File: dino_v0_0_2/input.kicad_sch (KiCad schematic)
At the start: 13 parts, among them SW1 SW_DIP_x08, U76 74LS138

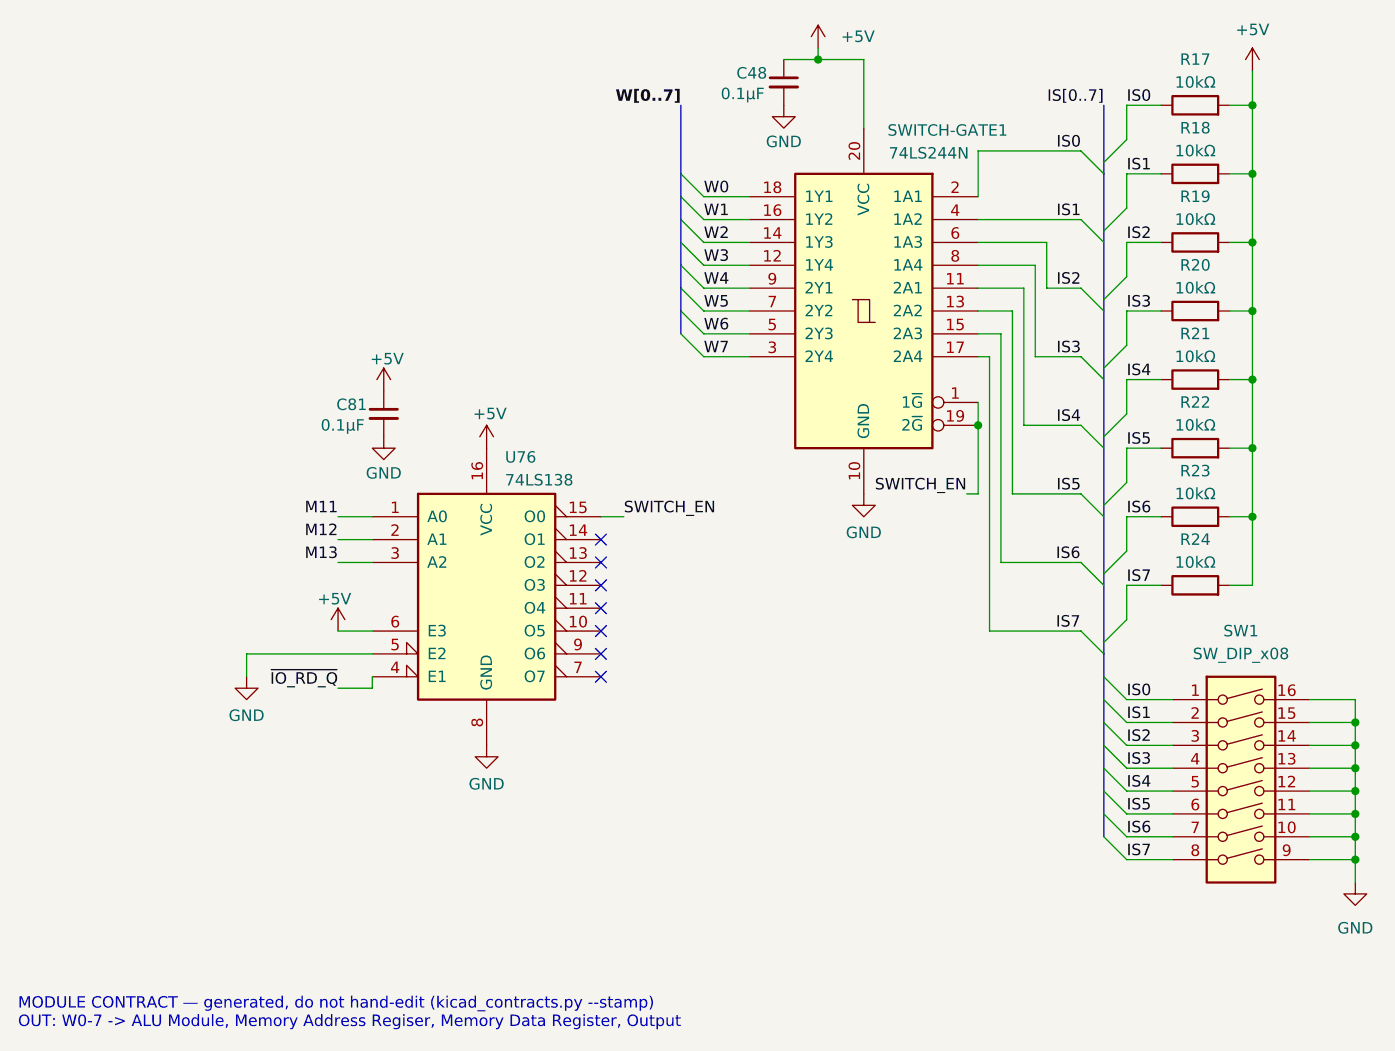
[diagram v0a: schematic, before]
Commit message: feat(kicad): footprints, power sheet, global labels, PCB draft
Every symbol gets a stock THT footprint (plain DIP, no sockets, so the
3D render shows ICs). New Power sheet: 24-pin ATX header for a picoPSU,
rails +5V/+3.3V/+12V/-12V/GND only; no -5V exists on any ATX unit since
2003, none drawn. PS_ON# on a 2-pin header.

Cross-sheet labels become global labels. KiCad joined nothing between
sheets before: 122 base names were split per sheet, ERC saw 90 undriven
inputs whose driver sat one sheet away, and the PCB ratsnest stopped at
every sheet boundary. Proof: KiCad's netlist after equals a name-join of
its netlist before plus the 15 CW alias pairs, pin for pin.

kicad_contracts took a node's sheet from the net name's /Sheet/ prefix;
global nets have none, so it emitted an empty contracts doc. Sheet now
comes from the component's own path; the doc regenerates with zero diff.

ERC 477 -> 2. Real fixes: ROM I/O pins input -> tri_state, '382 GND pin
power_out -> power_in, four orphan symbols rehomed to project lib `dino`,
one stub wire. 133 by-design warnings excluded by uuid ('245 readback on
counter Q, alias stubs, probe-point labels); the two left are bus
signals the peripheral bus sheet will consume.

PCB draft: 198 footprints placed per sheet, all pads netted, no tracks.

Co-Authored-By: Claude Fable 5.1 <noreply@anthropic.com>
Claude-Session: https://claude.ai/code/session_018irreFHb1xEykW5kCD26ow
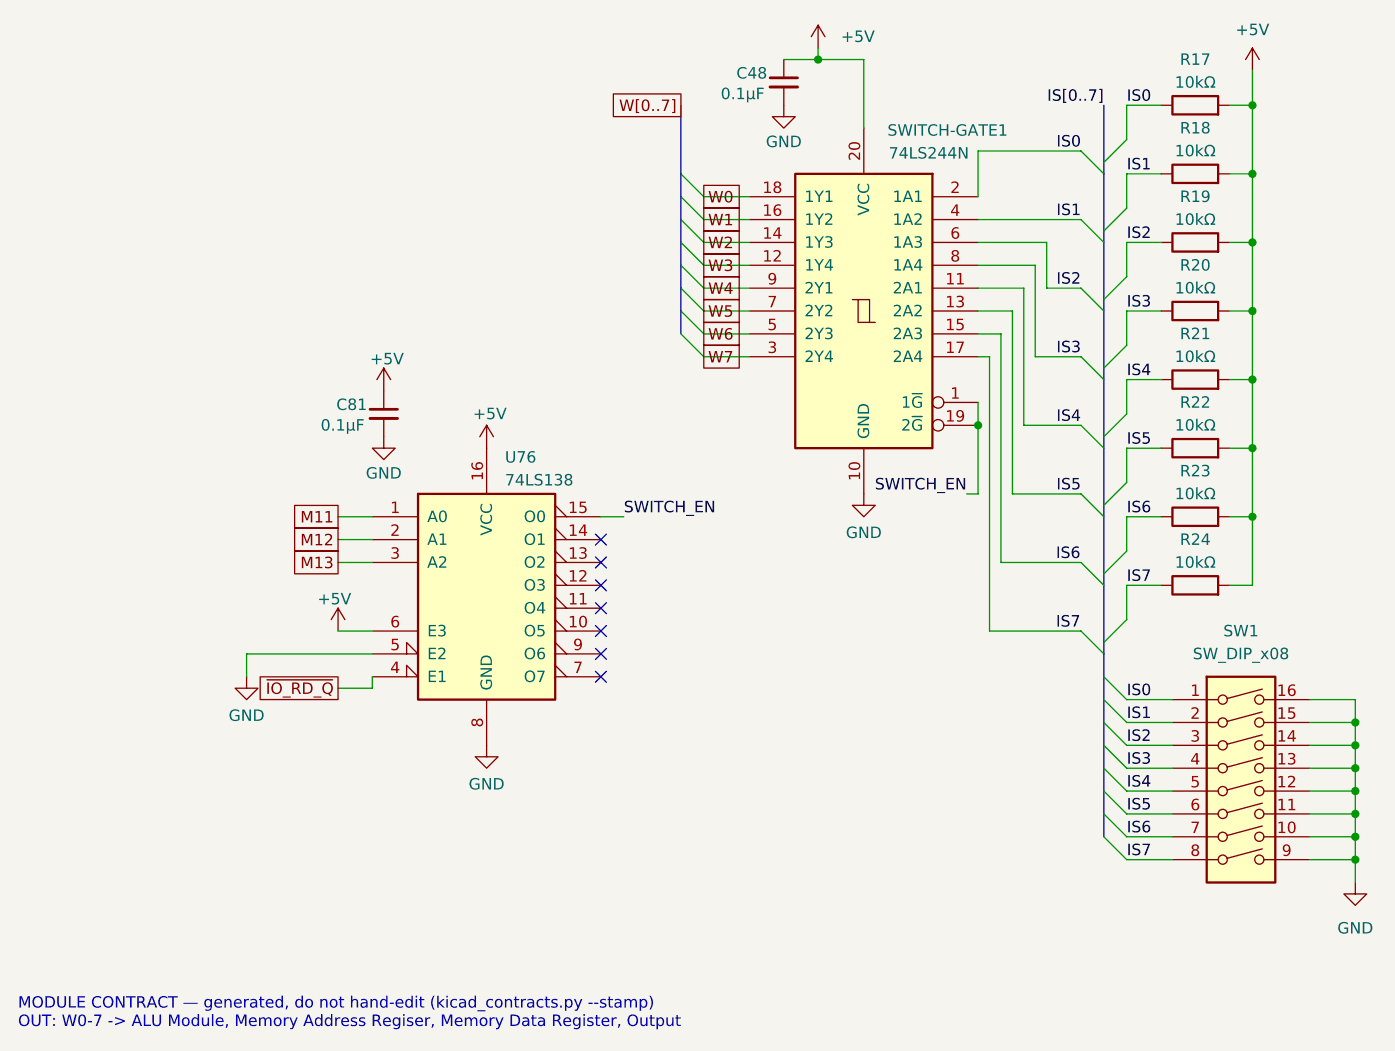
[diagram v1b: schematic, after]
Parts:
- C48, C81: footprint (none) -> Capacitor_THT:C_Disc_D5.0mm_W2.5mm_P2.50mm
- R17, R18, R19, R20, R21, R22, R23, R24: footprint (none) -> Resistor_THT:R_Axial_DIN0207_L6.3mm_D2.5mm_P10.16mm_Horizontal
- SW1: footprint (none) -> Button_Switch_THT:SW_DIP_SPSTx08_Slide_9.78x22.5mm_W7.62mm_P2.54mm
- SWITCH-GATE1: footprint (none) -> Package_DIP:DIP-20_W7.62mm; symbol 74xx:74LS244N -> dino:74LS244N
- U76: footprint (none) -> Package_DIP:DIP-16_W7.62mm
